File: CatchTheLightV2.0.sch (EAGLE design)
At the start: 42 parts, among them J1 TC2030-IDC-NL, U1 ATMEGA328PB-MUR

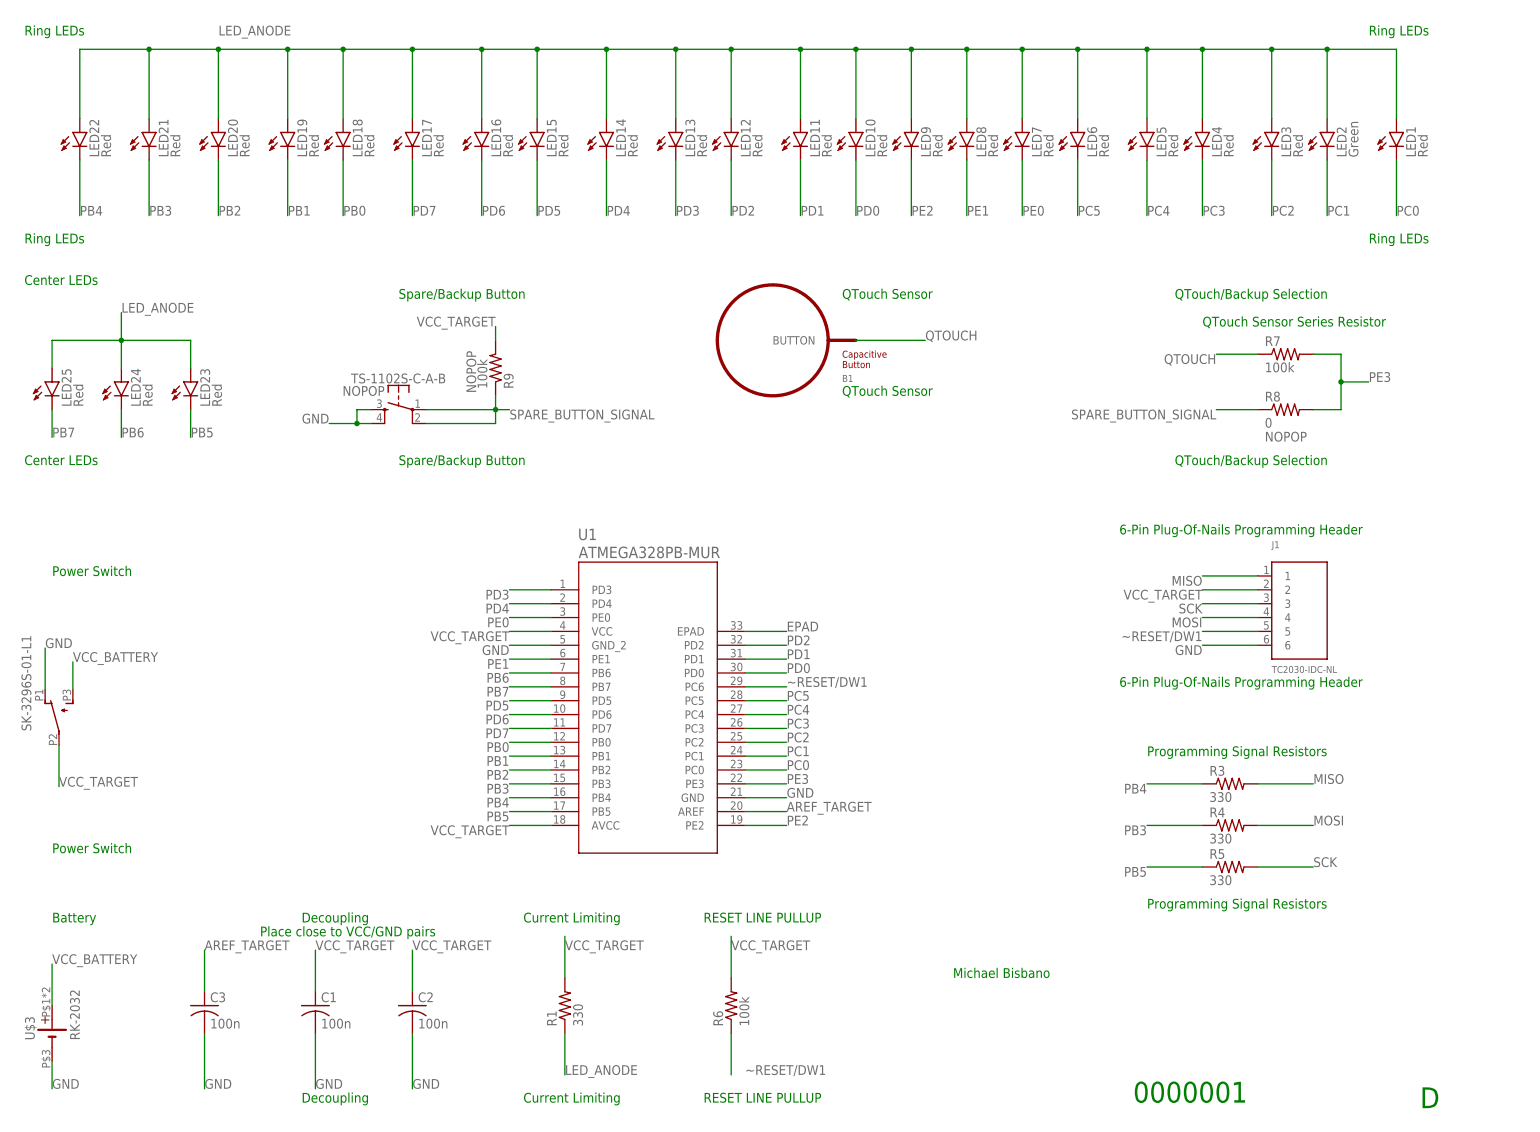
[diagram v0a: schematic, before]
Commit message: Revised Schematic and Board design to use correct 328pb footprint
Modified a whole lot. New approach to board design. Will try to fill in all wiring first, and then draw in the rest of the pours/planes
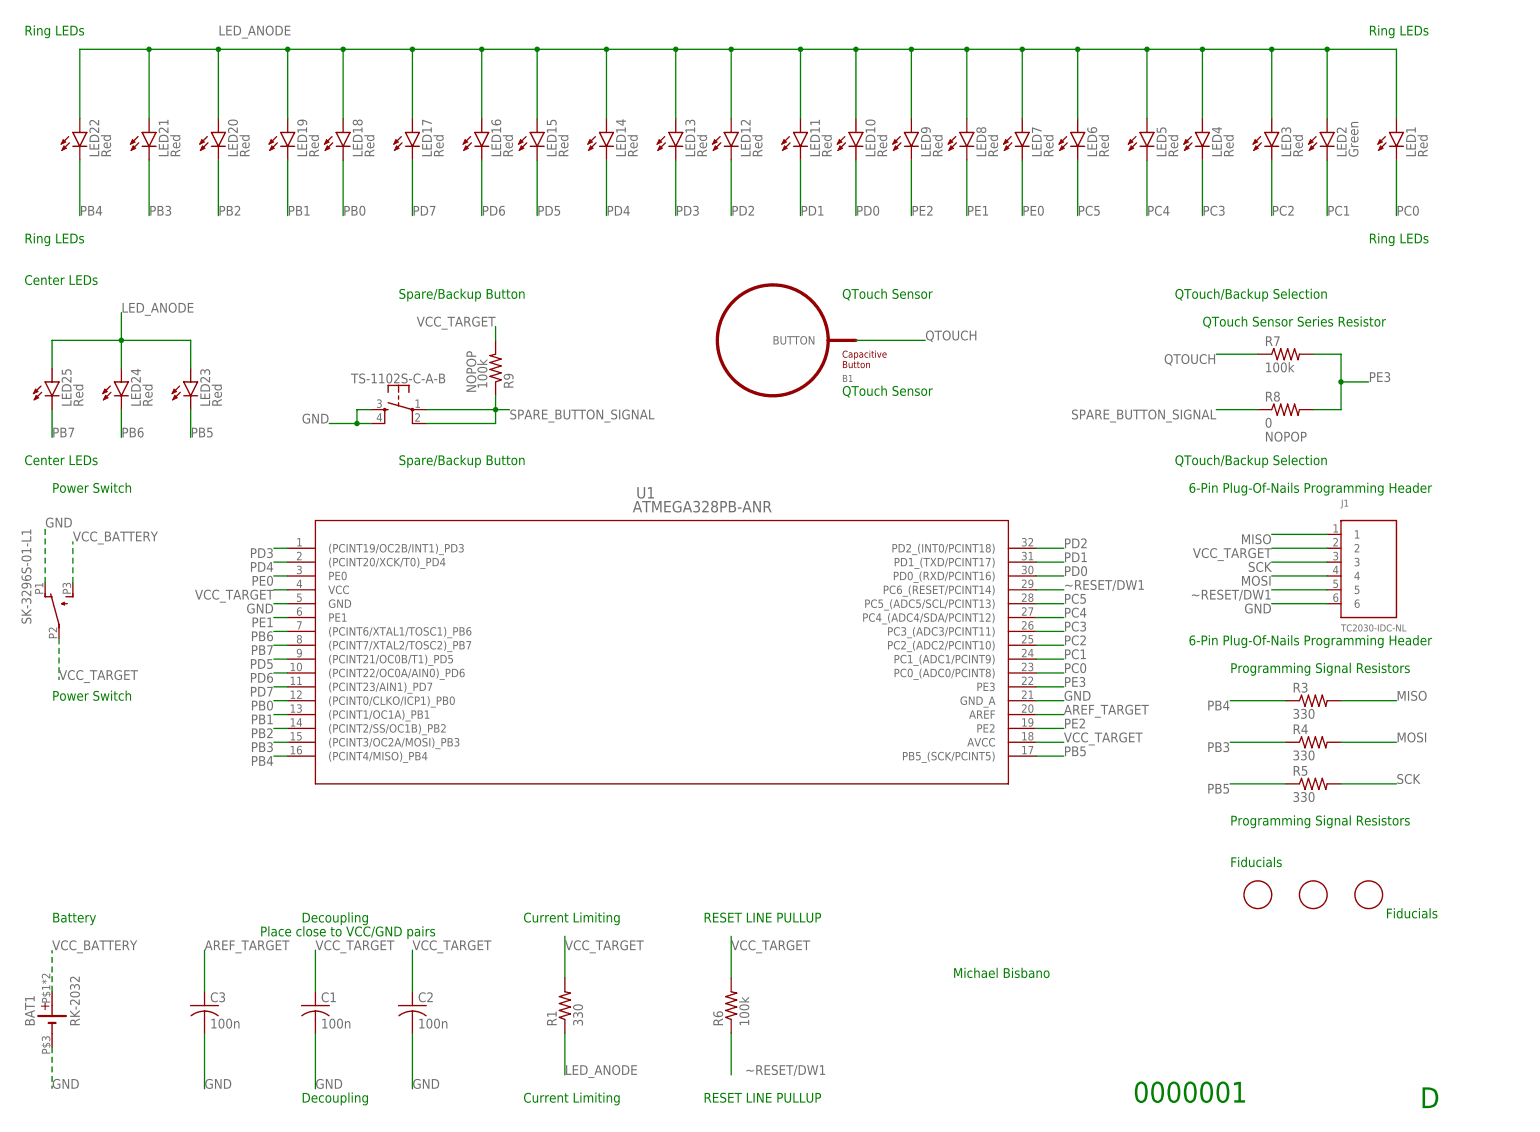
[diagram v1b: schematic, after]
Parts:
- removed U$1: SK-3296S-01-L1, CustomParts:SK-3296S-01-L1
- removed U$2: TS-1102S-C-A-B, CustomParts:TS-1102S-C-A-B
- removed U$3: RK-2032, CustomParts:RK-2032
- added BAT1: RK-2032, ECE_388_CustomParts_V1.1:RK-2032
- added PB1: SK-3296S-01-L1, ECE_388_CustomParts_V1.1:SK-3296S-01-L1
- added PB2: PB2, ECE_388_CustomParts_V1.1:TS-1102S-C-A-B
- added U$4, U$5, U$6: FIDUCIAL, ECE388:FIDUCIAL
- U1: value ATMEGA328PB-MUR -> ATMEGA328PB-ANR; device 328PBMUR:ATMEGA328PB-MUR -> ECE_388_CustomParts_V1.1:ATMEGA328PB-ANR
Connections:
- removed net EPAD: U1.EPAD
- net GND: now also BAT1.-, PB1.1, PB2.3, PB2.4, U1.GND_A; no longer U$1.1, U$2.3, U$2.4, U$3.-, U1.GND_2
- net PB0: now also U1.(PCINT0/CLKO/ICP1)_PB0; no longer U1.PB0
- net PB1: now also U1.(PCINT1/OC1A)_PB1; no longer U1.PB1
- net PB2: now also U1.(PCINT2/SS/OC1B)_PB2; no longer U1.PB2
- net PB3: now also U1.(PCINT3/OC2A/MOSI)_PB3; no longer U1.PB3
- net PB4: now also U1.(PCINT4/MISO)_PB4; no longer U1.PB4
- net PB5: now also U1.PB5_(SCK/PCINT5); no longer U1.PB5
- net PB6: now also U1.(PCINT6/XTAL1/TOSC1)_PB6; no longer U1.PB6
- net PB7: now also U1.(PCINT7/XTAL2/TOSC2)_PB7; no longer U1.PB7
- net PC0: now also U1.PC0_(ADC0/PCINT8); no longer U1.PC0
- net PC1: now also U1.PC1_(ADC1/PCINT9); no longer U1.PC1
- net PC2: now also U1.PC2_(ADC2/PCINT10); no longer U1.PC2
- net PC3: now also U1.PC3_(ADC3/PCINT11); no longer U1.PC3
- net PC4: now also U1.PC4_(ADC4/SDA/PCINT12); no longer U1.PC4
- net PC5: now also U1.PC5_(ADC5/SCL/PCINT13); no longer U1.PC5
- net PD0: now also U1.PD0_(RXD/PCINT16); no longer U1.PD0
- net PD1: now also U1.PD1_(TXD/PCINT17); no longer U1.PD1
- net PD2: now also U1.PD2_(INT0/PCINT18); no longer U1.PD2
- net PD3: now also U1.(PCINT19/OC2B/INT1)_PD3; no longer U1.PD3
- net PD4: now also U1.(PCINT20/XCK/T0)_PD4; no longer U1.PD4
- net PD5: now also U1.(PCINT21/OC0B/T1)_PD5; no longer U1.PD5
- net PD6: now also U1.(PCINT22/OC0A/AIN0)_PD6; no longer U1.PD6
- net PD7: now also U1.(PCINT23/AIN1)_PD7; no longer U1.PD7
- net SPARE_BUTTON_SIGNAL: now also PB2.1, PB2.2; no longer U$2.1, U$2.2
- net VCC_BATTERY: now also BAT1.+, PB1.3; no longer U$1.3, U$3.+
- net VCC_TARGET: now also PB1.2; no longer U$1.2
- net ~RESET/DW1: now also U1.PC6_(RESET/PCINT14); no longer U1.PC6
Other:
- note added: "Fiducials"
- moved on the sheet: J1, R3, R4, R5

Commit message: Schematic pdf updated and put in renders
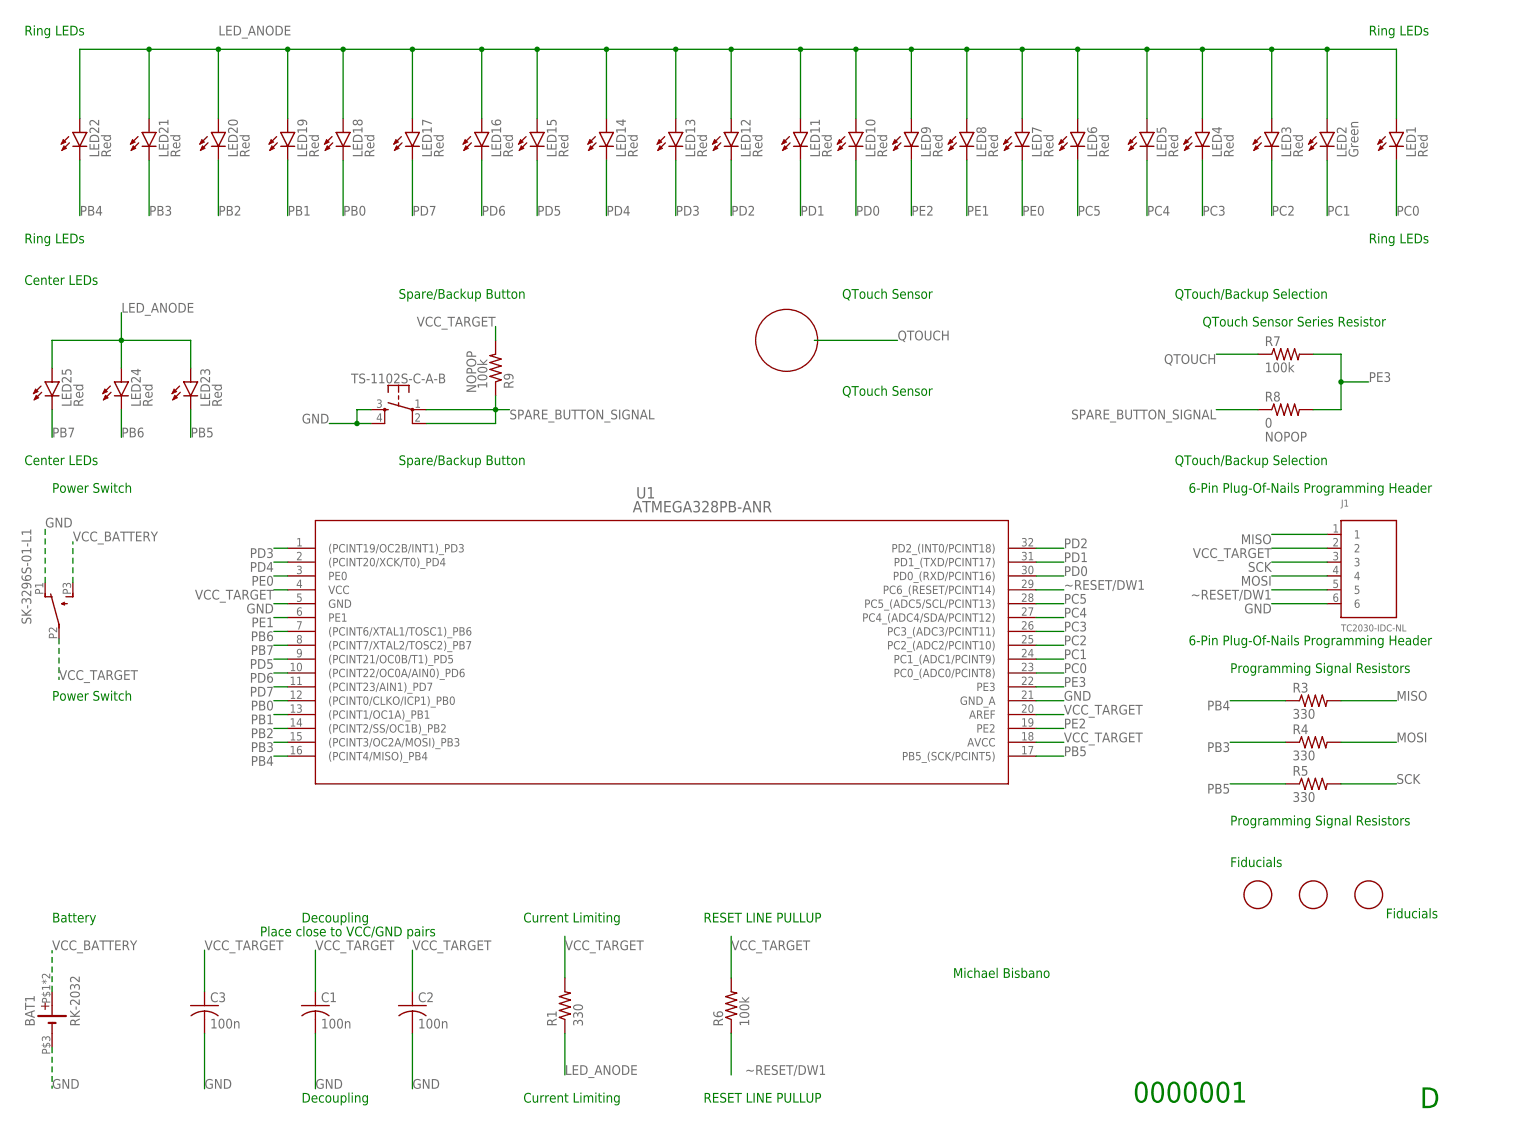
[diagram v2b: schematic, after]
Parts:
- removed B1: (no value), PatternAgents-TouchWidgets:BUTTON_PASSIVE12MM
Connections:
- removed net AREF_TARGET: C3.1, U1.AREF
- net QTOUCH: no longer B1.BUTTON
- net VCC_TARGET: now also C3.1, U1.AREF
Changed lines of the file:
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@@
 <part name="LED24" library="led" library_urn="urn:adsk.eagle:library:259" deviceset="LED" device="CHIP-LED0805" package3d_urn="urn:adsk.eagle:package:15818/2" value="Red"/>
 <part name="LED25" library="led" library_urn="urn:adsk.eagle:library:259" deviceset="LED" device="CHIPLED_0805" package3d_urn="urn:adsk.eagle:package:15821/2" value="Red"/>
-<part name="B1" library="PatternAgents-TouchWidgets" deviceset="BUTTON_PASSIVE" device="12MM"/>
 <part name="R8" library="rcl" library_urn="urn:adsk.eagle:library:334" deviceset="R-US_" device="R0805" package3d_urn="urn:adsk.eagle:package:23553/2" value="0">
 <spice>
@@
 <text x="231.14" y="-165.1" size="1.778" layer="91">Fiducials</text>
 <text x="269.24" y="-172.72" size="1.778" layer="91" rot="R180">Fiducials</text>
+<circle x="149.86" y="-68.58" radius="5.6796125" width="0.1524" layer="94"/>
 </plain>
 <instances>
@@
 <attribute name="NAME" x="18.796" y="-80.772" size="1.778" layer="95" rot="R90"/>
 <attribute name="VALUE" x="20.955" y="-80.772" size="1.778" layer="96" rot="R90"/>
-</instance>
-<instance part="B1" gate="B1" x="147.32" y="-68.58" smashed="yes">
-<attribute name="NAME" x="160.02" y="-76.2" size="1.27" layer="95" font="vector" ratio="15"/>
-<attribute name="VALUE" x="160.02" y="-78.74" size="1.27" layer="96" font="vector" ratio="15"/>
 </instance>
 <instance part="R8" gate="G$1" x="241.3" y="-81.28" smashed="yes">
@@
 <label x="16.51" y="-130.81" size="1.778" layer="95"/>
 </segment>
-</net>
-<net name="AREF_TARGET" class="0">
+<segment>
+<wire x1="195.58" y1="-137.16" x2="200.66" y2="-137.16" width="0.1524" layer="91"/>
+<label x="200.66" y="-137.16" size="1.778" layer="95"/>
+<pinref part="U1" gate="A" pin="AREF"/>
+</segment>
 <segment>
 <pinref part="C3" gate="G$1" pin="1"/>
@@
 <label x="43.18" y="-180.34" size="1.778" layer="95"/>
 </segment>
-<segment>
-<wire x1="195.58" y1="-137.16" x2="200.66" y2="-137.16" width="0.1524" layer="91"/>
-<label x="200.66" y="-137.16" size="1.778" layer="95"/>
-<pinref part="U1" gate="A" pin="AREF"/>
-</segment>
 </net>
 <net name="PE2" class="0">
@@
 </segment>
 <segment>
-<pinref part="B1" gate="B1" pin="BUTTON"/>
-<wire x1="162.56" y1="-68.58" x2="175.26" y2="-68.58" width="0.1524" layer="91"/>
-<label x="175.26" y="-68.58" size="1.778" layer="95"/>
+<wire x1="154.94" y1="-68.58" x2="170.18" y2="-68.58" width="0.1524" layer="91"/>
+<label x="170.18" y="-68.58" size="1.778" layer="95"/>
 </segment>
 </net>
@@
 </drawing>
 <compatibility>
-<note version="6.3" minversion="6.2.2" severity="warning">
-Since Version 6.2.2 text objects can contain more than one line,
-which will not be processed correctly with this version.
-</note>
 <note version="8.2" severity="warning">
 Since Version 8.2, EAGLE supports online libraries. The ids

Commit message: Schematic Submission Issues addressed
Changes documented in issue
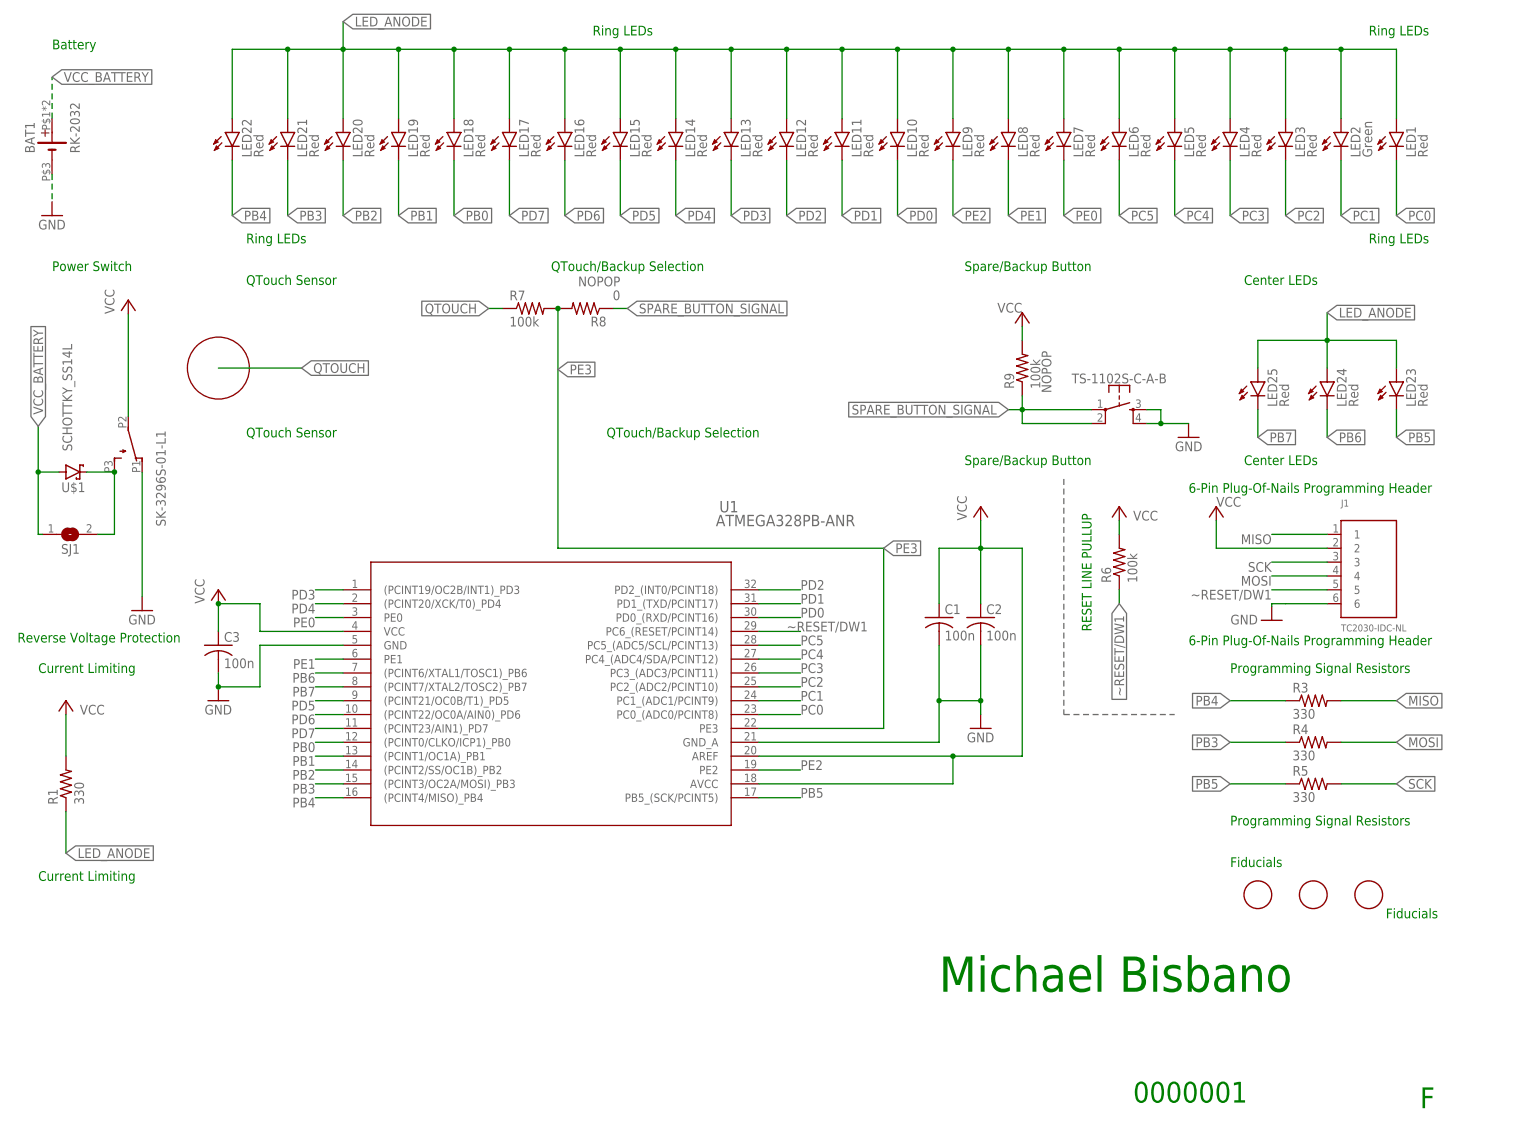
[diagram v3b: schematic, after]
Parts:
- added SJ1: (no value), ECE388:SJW
- added U$1: SCHOTTKY_SS14L, ECE_388_CustomParts_V1.1:SCHOTTKY_SS14L
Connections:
- net VCC_TARGET renamed VCC
- new net PROTECTED_VBAT: PB1.3, SJ1.2, U$1.C
- net VCC_BATTERY: now also SJ1.1, U$1.A; no longer PB1.3
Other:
- note added: "F"
- note added: "Reverse Voltage Protection"
- note removed: "D"
- note removed: "Decoupling"
- note removed: "Place close to VCC/GND pairs"
- note removed: "QTouch Sensor Series Resistor"
- moved on the sheet: BAT1, C1, C2, C3, LED10, LED11, LED12, LED13, LED14, LED15, LED16, LED17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
